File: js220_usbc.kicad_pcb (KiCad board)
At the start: 4 copper layers, 95 x 24.7 mm, 14 parts, among them J1 JS220, J2 USB_C_Receptacle, J3 USB_C_Receptacle

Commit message: Fix polarity...
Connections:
- J1 pad 1: /VBUS_DEV -> /VBUS_SRC
- J1 pad 2: /VBUS_DEV -> /VBUS_SRC
- J1 pad 3: /VBUS_SRC -> /VBUS_DEV
- J1 pad 4: /VBUS_SRC -> /VBUS_DEV
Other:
- board text added: "v1.1"
- board text removed: "v1.0"

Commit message: Update readme and silkscreen/version
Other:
- board text added: "alvarop.com"
- board text removed: "by @alvaroprieto"
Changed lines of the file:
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@@
     (effects (font (size 2 2) (thickness 0.3)) (justify mirror))
   )
-  (gr_text "by @alvaroprieto" (at 121.5 109.5) (layer "B.SilkS")
+  (gr_text "alvarop.com" (at 119.05 109.5) (layer "B.SilkS")
     (effects (font (size 1 1) (thickness 0.15)) (justify mirror))
   )

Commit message: v1.2 Done
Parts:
- added SW1: SW_DPDT_x2, snapeda:SW_JS202011SCQN, F.Cu at (175.0, 100.0)
- moved C2 28.3 mm to (178.6, 102.8), turned to 0 degrees
- moved C1 27.9 mm to (178.5, 97.3), turned to 0 degrees
- moved R2 1.48 mm to (150.0, 107.8)
- moved R1 0.73 mm to (149.1, 93.0)
- turned J3 to 180 degrees
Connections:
- C1 pad 1: /CC1_DEV -> Net-(C1-Pad1)
- C2 pad 1: /CC2_DEV -> Net-(C2-Pad1)
- J3 pad A10: /RX2- -> /TX2-
- J3 pad A11: /RX2+ -> /TX2+
- J3 pad A2: /TX1+ -> /RX1+
- J3 pad A3: /TX1- -> /RX1-
- J3 pad A8: /SBU1 -> /SBU2
- J3 pad B10: /RX1- -> /TX1-
- J3 pad B11: /RX1+ -> /TX1+
- J3 pad B2: /TX2+ -> /RX2+
- J3 pad B3: /TX2- -> /RX2-
- J3 pad B8: /SBU2 -> /SBU1
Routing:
- net /CC1_DEV: track 14.3 -> 34.7 mm, vias 1 -> 2
- net /CC2_DEV: track 19.0 -> 39.4 mm, vias 3 -> 2
- net /RX2+: track 40.1 -> 23.0 mm, vias 2 -> 0
- net /RX2-: track 39.7 -> 23.7 mm, vias 2 -> 0
- net /SHLD_SRC: track 27.1 -> 14.1 mm
- net /SBU1: track 36.1 -> 26.9 mm, vias 2 -> 0
- net /SHLD_DEV: track 17.3 -> 8.15 mm
- net /B_D+: track 36.5 -> 28.8 mm
- net /B_D-: track 36.9 -> 29.6 mm
- net /RX1-: track 40.4 -> 33.2 mm, vias 2 -> 0
- net /SBU2: track 37.6 -> 30.8 mm, vias 2 -> 0
- net /RX1+: track 40.8 -> 34.3 mm, vias 2 -> 0
- net /TX2+: track 33.8 -> 27.3 mm, vias 2 -> 0
- net /TX2-: track 34.2 -> 28.0 mm, vias 2 -> 0
- net /A_D-: track 35.3 -> 30.7 mm
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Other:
- board text added: "OFF"
- board text added: "ON"
- board text added: "USB-PD"
- board text added: "WARNING: Voltages Higher than 15V may be present if USB-PD is enabled!"
- board text added: "v1.2"
- board text removed: "v1.1"

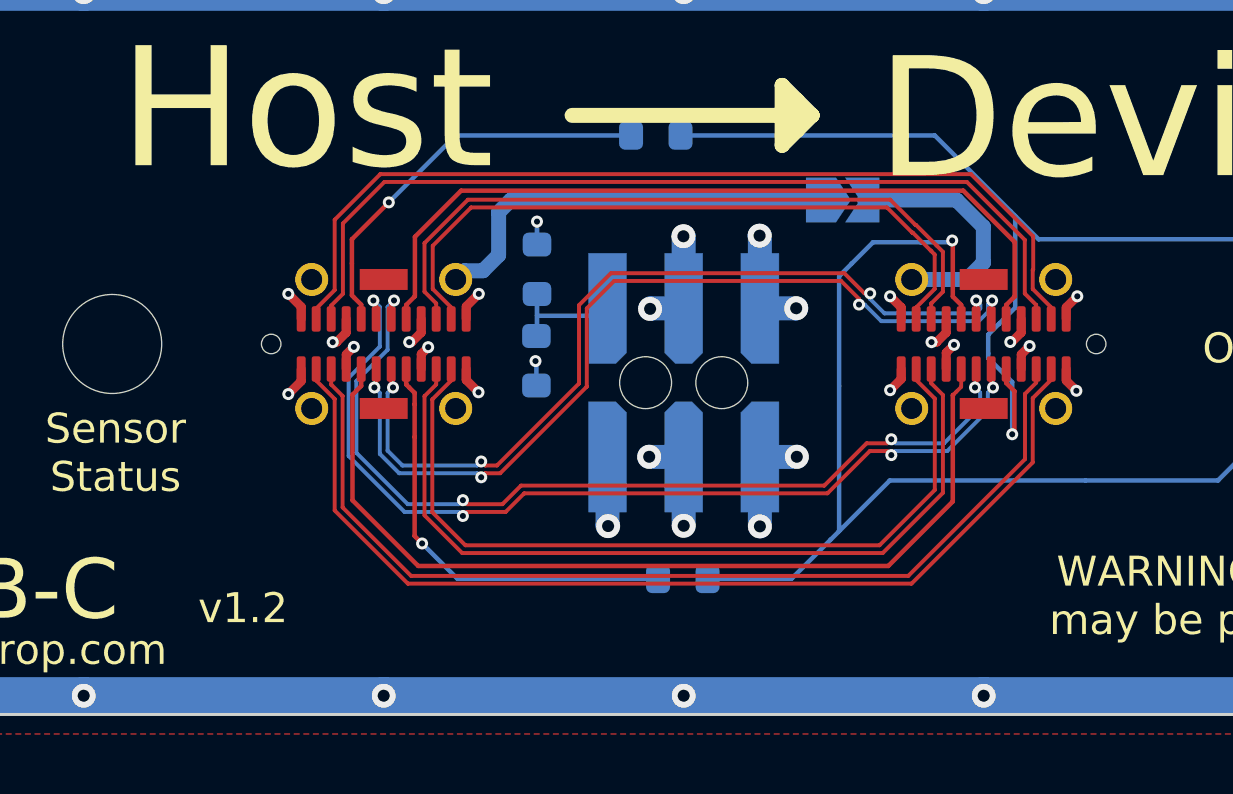
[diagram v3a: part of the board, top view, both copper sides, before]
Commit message: Fixed length matching for v1.3
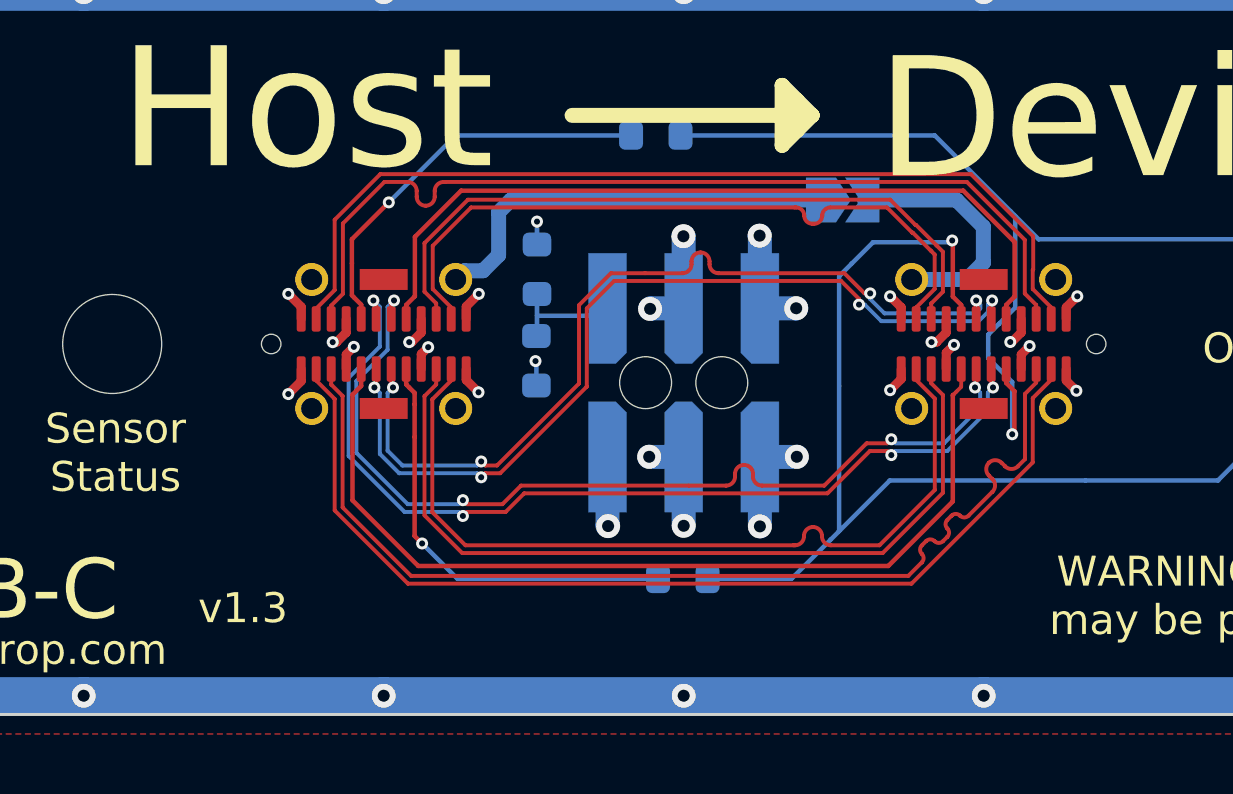
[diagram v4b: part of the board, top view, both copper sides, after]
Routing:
- net /RX1-: track 33.2 -> 35.1 mm
- net /TX1-: track 30.2 -> 31.3 mm
- net /B_D+: track 28.8 -> 29.6 mm
- net /A_D-: track 30.7 -> 31.5 mm
- net /TX2+: track 27.3 -> 27.9 mm
- net /RX2+: track 23.0 -> 23.6 mm
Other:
- board text added: "v1.3"
- board text removed: "v1.2"
